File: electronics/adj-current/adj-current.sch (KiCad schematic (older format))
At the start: 9 parts, among them J1 Power, J2 Output, Q1 IRLZ44N, U1 LM358, U2 TL431DBZ

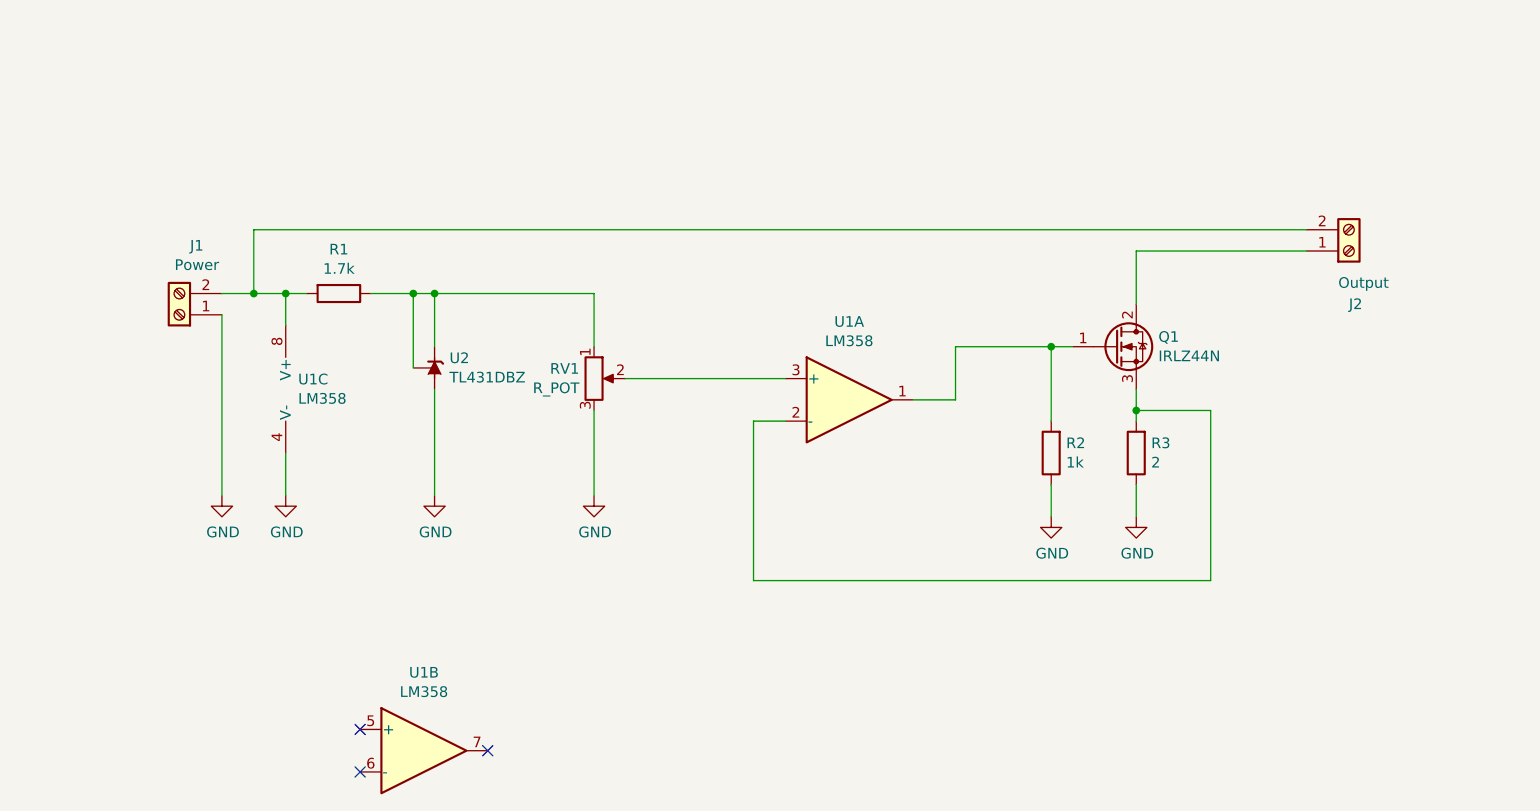
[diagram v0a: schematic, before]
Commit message: adj current driver
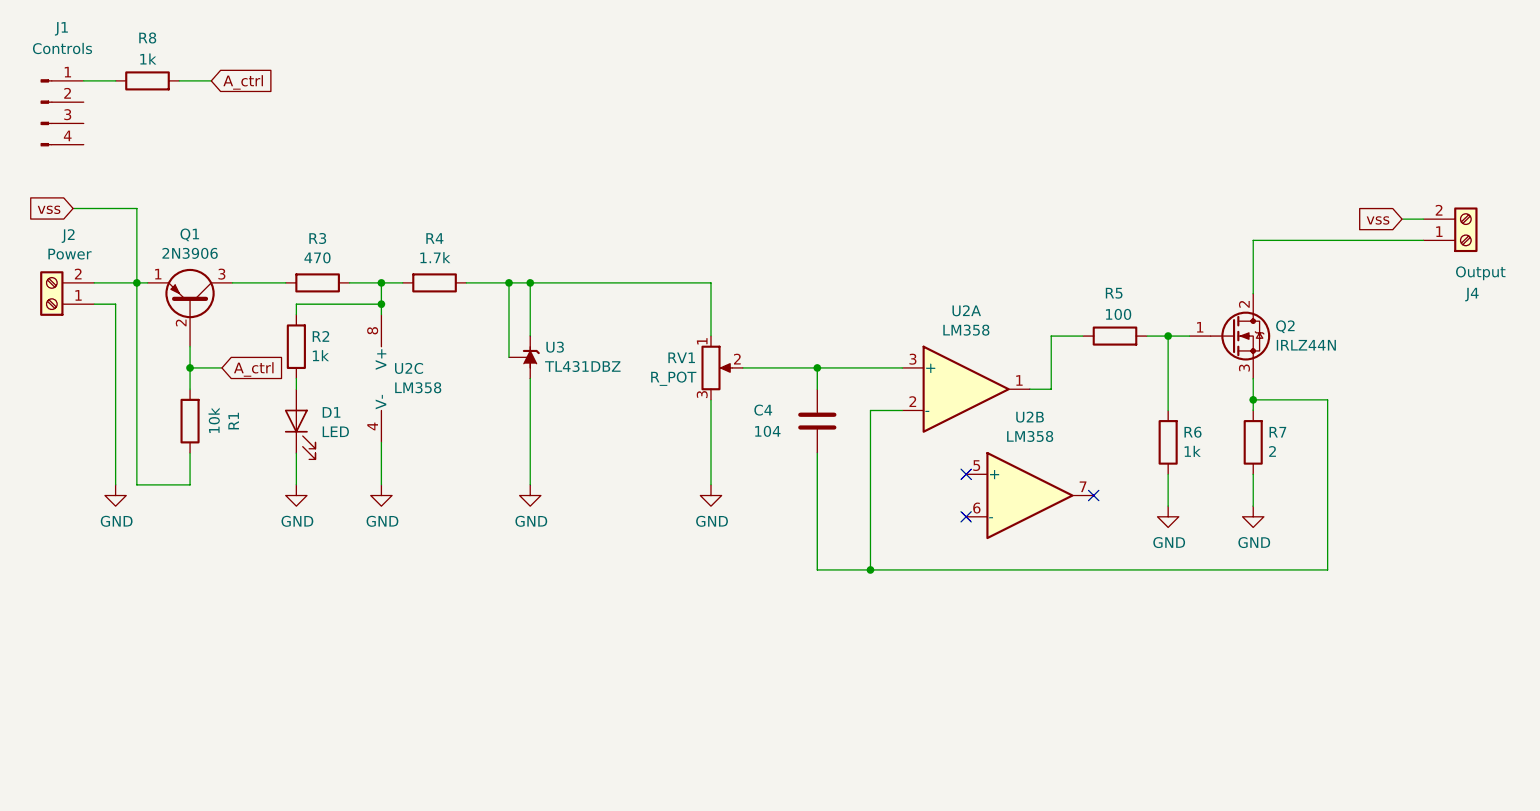
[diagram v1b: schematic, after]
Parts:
- added C4: 104, Capacitor_THT:C_Disc_D7.0mm_W2.5mm_P5.00mm, symbol Device:C
- added D1: LED, LED_THT:LED_D3.0mm, symbol Device:LED
- added J1: Controls, Connector_PinHeader_2.54mm:PinHeader_1x04_P2.54mm_Vertical, symbol Connector:Conn_01x04_Male
- added Q1: 2N3906, Package_TO_SOT_THT:TO-92_Inline, symbol Transistor_BJT:2N3906
- added R1: 10k, Resistor_THT:R_Axial_DIN0204_L3.6mm_D1.6mm_P7.62mm_Horizontal, symbol Device:R
- added R2, R8: 1k, Resistor_THT:R_Axial_DIN0204_L3.6mm_D1.6mm_P7.62mm_Horizontal, symbol Device:R
- added R3: 470, Resistor_THT:R_Axial_DIN0204_L3.6mm_D1.6mm_P7.62mm_Horizontal, symbol Device:R
- added R5: 100, Resistor_THT:R_Axial_DIN0204_L3.6mm_D1.6mm_P7.62mm_Horizontal, symbol Device:R
- renumbered J1 to J2, J2 to J4, Q1 to Q2, R1 to R4, R2 to R6, R3 to R7, U1 to U2, U2 to U3
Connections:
- net GND: now also D1.1 (K)
- net at R4.2, U2.8 (V+): now also R2.2, R3.1; no longer J2.2 (Pin_2), J4.2 (Pin_2)
- net at Q2.1 (G), R6.2: now also R5.2; no longer U2.1
- net at Q2.3 (S), R7.2, U2.2 (-): now also C4.2
- net at RV1.2, U2.3 (+): now also C4.1
- new net: R5.1, U2.1
- new net: J1.1 (Pin_1), R8.1
- new net: Q1.3 (C), R3.2
- new net: D1.2 (A), R2.1
- new net A_ctrl: Q1.2 (B), R1.2, R8.2
- new net vss: J2.2 (Pin_2), J4.2 (Pin_2), Q1.1 (E), R1.1
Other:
- moved on the sheet: J2, J4, Q2, R4, R6, R7, RV1, U2A, U2B, U2C, U3
